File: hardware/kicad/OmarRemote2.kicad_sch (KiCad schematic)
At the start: 17 parts, among them J1 Conn_01x02_Pin, SW1 SW_Push, SW2 SW_Push, SW3 SW_Push, SW4 SW_Push, SW5 SW_Push, SW6 SW_Push, U1 XIAO-ESP32-S3-SMD

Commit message: further work on TP4056 footprint
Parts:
- removed BC2: Battery Charger, symbol TP4056_USB-C_Protect_Module:TP4056_USB-C_Protect_Module
- added BC1: Battery Charger, symbol TP4056_USB-C_Protect_Module:TP4056_USB-C_Protect_Module
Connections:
- net BAT+: now also BC1. (OUT-); no longer R4.2, U1.15 (BAT)
- net BAT-: now also BC1. (OUT-); no longer R3.1, U1.16 (GND)
- new net OUT+: BC1. (OUT-), R4.2, U1.15 (BAT)
- new net OUT-: BC1. (OUT-), R3.1, U1.16 (GND)
- no-connect marks 2 -> 0

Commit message: update libaries
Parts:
- removed IR1: KY-005, symbol KY-005_IR:KY-005_IR_Sender
- removed U1: XIAO-ESP32-S3-SMD, symbol Seeed_Studio_XIAO_Series:XIAO-ESP32-C6-SMD
- added IR?: KY-005, symbol CustomLibary:KY-005_IR_Sender
- added U?: XIAO-ESP32-S3-SMD, CustomLibrary:XIAO-ESP32C6-SMD, symbol CustomLibary:XIAO-ESP32-C6-SMD
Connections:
- net 5V: now also IR?.2 (Vcc), U?.14 (5V)
- net ButtonBACK: now also U?.2 (GPIO1_A1_D1)
- net ButtonDOWN: now also U?.4 (GPIO21_D3)
- net ButtonLEFT: now also U?.6 (GPIO23_D5_SCL)
- net ButtonOK: now also U?.1 (GPIO0_A0_D0)
- net ButtonRIGHT: now also U?.5 (GPIO22_D4_SDA)
- net ButtonUP: now also U?.3 (GPIO2_A2_D2)
- net GND: now also IR?.3 (GND), U?.13 (GND)
- net IR: now also IR?.1 (INPUT), U?.7 (GPIO16_D6_TX)
- net LEDCharge: now also U?.9 (GPIO19_D8_SCK)
- net LEDPower: now also U?.8 (GPIO17_D7_RX)
- net OUT+: now also U?.15 (BAT)
- net OUT-: now also U?.16 (GND)
- net VoltBattery: now also U?.10 (GPIO20_D9_MISO)
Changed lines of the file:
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@@
+	)
+	(symbol
+		(lib_id "CustomLibary:XIAO-ESP32-C6-SMD")
+		(at 143.51 52.07 0)
+		(unit 1)
+		(exclude_from_sim no)
+		(in_bom yes)
+		(on_board yes)
+		(dnp no)
+		(fields_autoplaced yes)
+		(property "Reference" "U?"
+			(at 148.1933 73.66 0)
+			(effects
+				(font
+					(size 1.27 1.27)
+				)
+				(justify left)
+			)
+		)
+		(property "Value" "XIAO-ESP32-S3-SMD"
+			(at 148.1933 76.2 0)
+			(effects
+				(font
+					(size 1.27 1.27)
+				)
+				(justify left)
+			)
+		)
+		(property "Footprint" "CustomLibrary:XIAO-ESP32C6-SMD"
+			(at 134.62 46.99 0)
+			(effects
+				(font
+					(size 1.27 1.27)
+				)
+				(hide yes)
+			)
+		)
+		(property "Datasheet" ""
+			(at 134.62 46.99 0)
+			(effects
+				(font
+					(size 1.27 1.27)
+				)
+				(hide yes)
+			)
+		)
+		(property "Description" ""
+			(at 143.51 52.07 0)
+			(effects
+				(font
+					(size 1.27 1.27)
+				)
+				(hide yes)
+			)
+		)
+		(pin "22"
+		)
+		(pin "16"
+		)
+		(pin "21"
+		)
+		(pin "20"
+		)
+		(pin "15"
+		)
+		(pin "19"
+		)
+		(pin "18"
+		)
+		(pin "17"
+		)
+		(pin "7"
+		)
+		(pin "6"
+		)
+		(pin "5"
+		)
+		(pin "4"
+		)
+		(pin "3"
+		)
+		(pin "2"
+		)
+		(pin "1"
+		)
+		(pin "24"
+		)
+		(pin "14"
+		)
+		(pin "13"
+		)
+		(pin "12"
+		)
+		(pin "23"
+		)
+		(pin "11"
+		)
+		(pin "10"
+		)
+		(pin "9"
+		)
+		(pin "8"
+		)
+		(instances
+			(project ""
+				(path "/1bf0dd3a-ef06-4d9e-bc1a-d833f6081a87"
+					(reference "U?")
+					(unit 1)
+				)
+			)
+		)
 	)
 	(symbol
@@
 	)
 	(symbol
-		(lib_id "Seeed_Studio_XIAO_Series:XIAO-ESP32-C6-SMD")
-		(at 143.51 52.07 0)
-		(unit 1)
-		(exclude_from_sim no)
-		(in_bom yes)
-		(on_board yes)
-		(dnp no)
-		(fields_autoplaced yes)
-		(property "Reference" "U1"
-			(at 148.1933 73.66 0)
-			(effects
-				(font
-					(size 1.27 1.27)
-				)
-				(justify left)
-			)
-		)
-		(property "Value" "XIAO-ESP32-S3-SMD"
-			(at 148.1933 76.2 0)
-			(effects
-				(font
-					(size 1.27 1.27)
-				)
-				(justify left)
-			)
-		)
-		(property "Footprint" ""
-			(at 134.62 46.99 0)
-			(effects
-				(font
-					(size 1.27 1.27)
-				)
-				(hide yes)
-			)
-		)
-		(property "Datasheet" ""
-			(at 134.62 46.99 0)
-			(effects
-				(font
-					(size 1.27 1.27)
-				)
-				(hide yes)
-			)
-		)
-		(property "Description" ""
-			(at 143.51 52.07 0)
-			(effects
-				(font
-					(size 1.27 1.27)
-				)
-				(hide yes)
-			)
-		)
-		(pin "23"
-		)
-		(pin "3"
-		)
-		(pin "10"
-		)
-		(pin "1"
-		)
-		(pin "17"
-		)
-		(pin "22"
-		)
-		(pin "2"
-		)
-		(pin "11"
-		)
-		(pin "13"
-		)
-		(pin "4"
-		)
-		(pin "16"
-		)
-		(pin "20"
-		)
-		(pin "7"
-		)
-		(pin "5"
-		)
-		(pin "6"
-		)
-		(pin "19"
-		)
-		(pin "8"
-		)
-		(pin "9"
-		)
-		(pin "15"
-		)
-		(pin "14"
-		)
-		(pin "18"
-		)
-		(pin "24"
-		)
-		(pin "12"
-		)
-		(pin "21"
-		)
-		(instances
-			(project ""
-				(path "/1bf0dd3a-ef06-4d9e-bc1a-d833f6081a87"
-					(reference "U1")
-					(unit 1)
-				)
-			)
-		)
-	)
-	(symbol
 		(lib_id "TP4056_USB-C_Protect_Module:TP4056_USB-C_Protect_Module")
 		(at 81.28 163.83 0)
@@
 	)
 	(symbol
-		(lib_id "KY-005_IR:KY-005_IR_Sender")
+		(lib_id "CustomLibary:KY-005_IR_Sender")
 		(at 129.54 105.41 0)
 		(unit 1)
@@
 		(dnp no)
 		(fields_autoplaced yes)
-		(property "Reference" "IR1"
+		(property "Reference" "IR?"
 			(at 135.89 100.33 0)
 			(effects
@@
 			)
 		)
-		(pin "1"
-		)
 		(pin "2"
 		)
 		(pin "3"
 		)
-		(instances
-			(project ""
-				(path "/1bf0dd3a-ef06-4d9e-bc1a-d833f6081a87"
-					(reference "IR1")
-					(unit 1)
-				)
+		(pin "1"
+		)
+		(instances
+			(project ""
+				(path "/1bf0dd3a-ef06-4d9e-bc1a-d833f6081a87"
+					(reference "IR?")
+					(unit 1)
+				)

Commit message: steal subsheets from @MayNiklas
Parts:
- removed J1: Conn_01x02_Pin, symbol Connector:Conn_01x02_Pin
- gave numbers to parts that had none: 2
- renumbered R3 to R1, R4 to R2, R1 to R3, R2 to R4
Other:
- added sheet USB-C charging (USB.kicad_sch)
- added sheet battery protection (battery_protection.kicad_sch)
- added sheet charging (charging.kicad_sch)

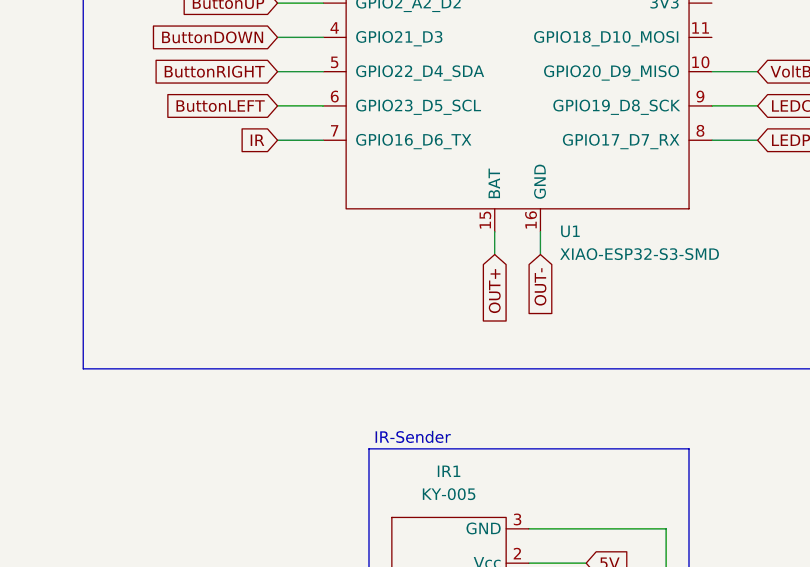
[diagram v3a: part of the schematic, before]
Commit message: add switch
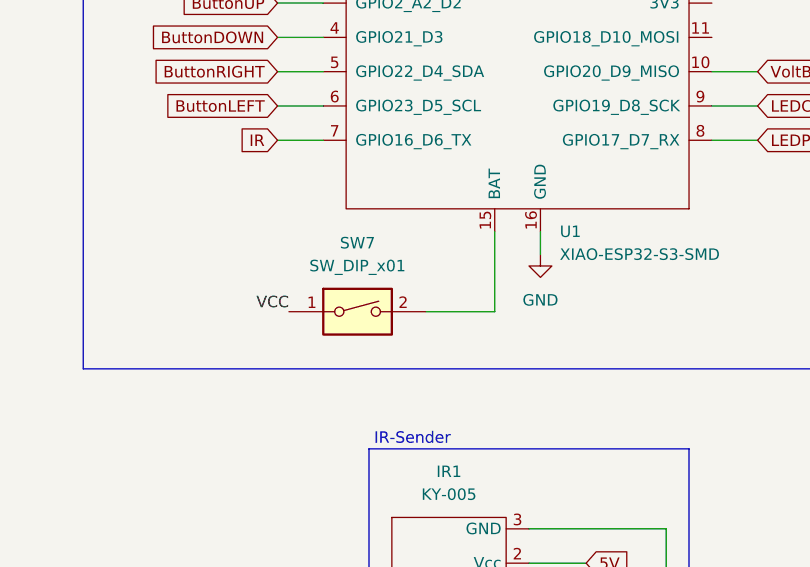
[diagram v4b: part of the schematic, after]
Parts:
- added SW7: SW_DIP_x01, symbol Switch:SW_DIP_x01
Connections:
- net GND: now also U1.16 (GND)
- net OUT+: no longer U1.15 (BAT)
- net OUT-: no longer U1.16 (GND)
- net VCC: now also SW7.1
- new net: SW7.2, U1.15 (BAT)

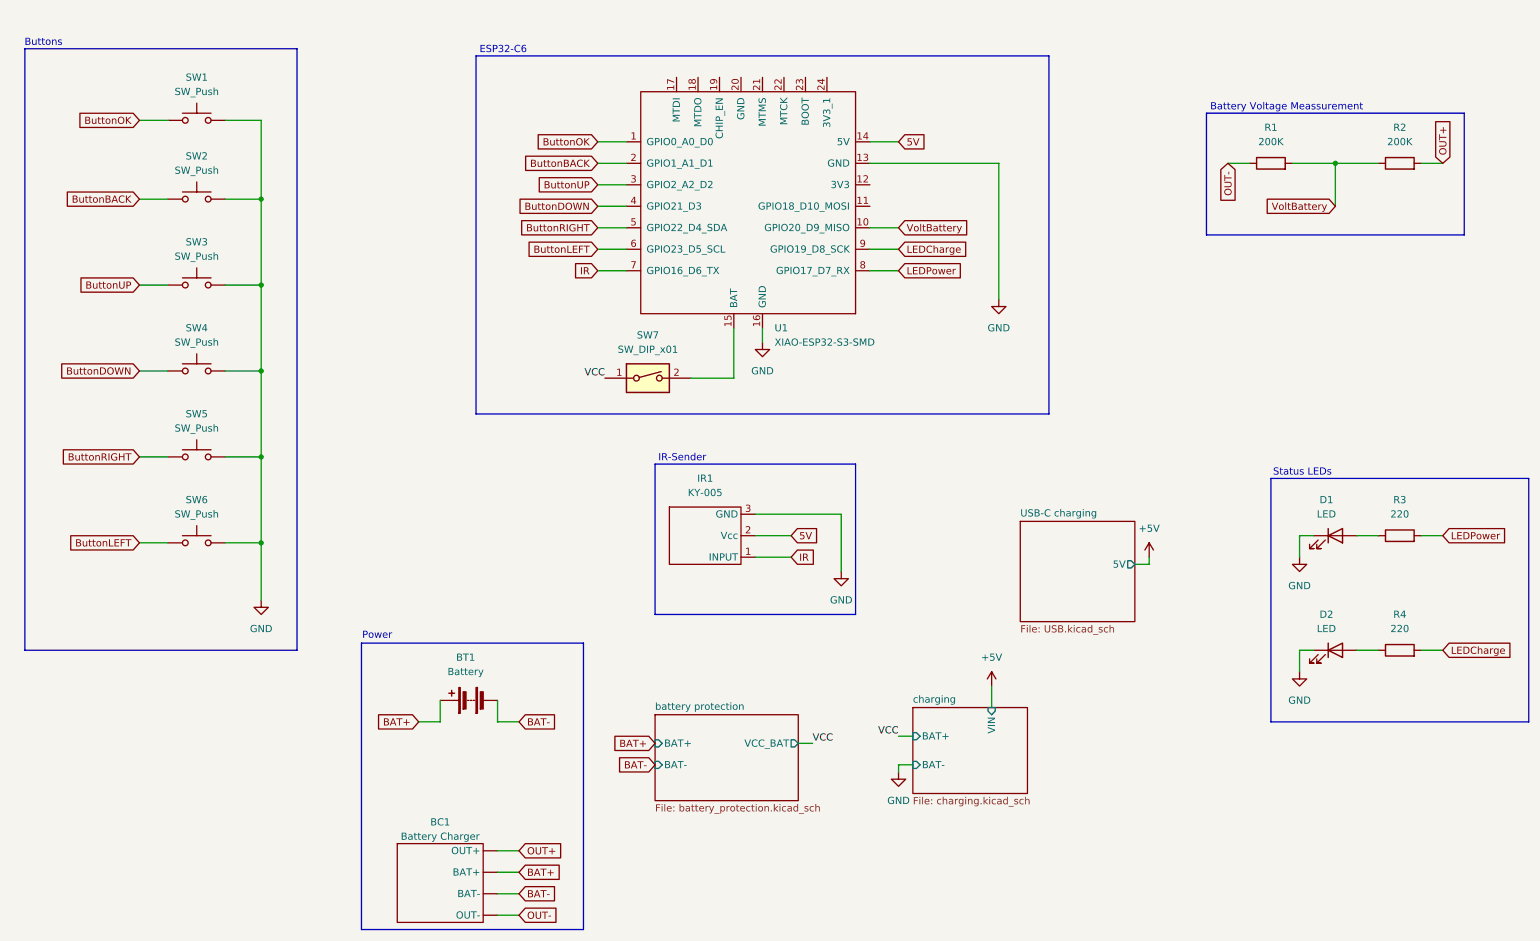
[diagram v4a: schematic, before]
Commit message: fix voltage measurement
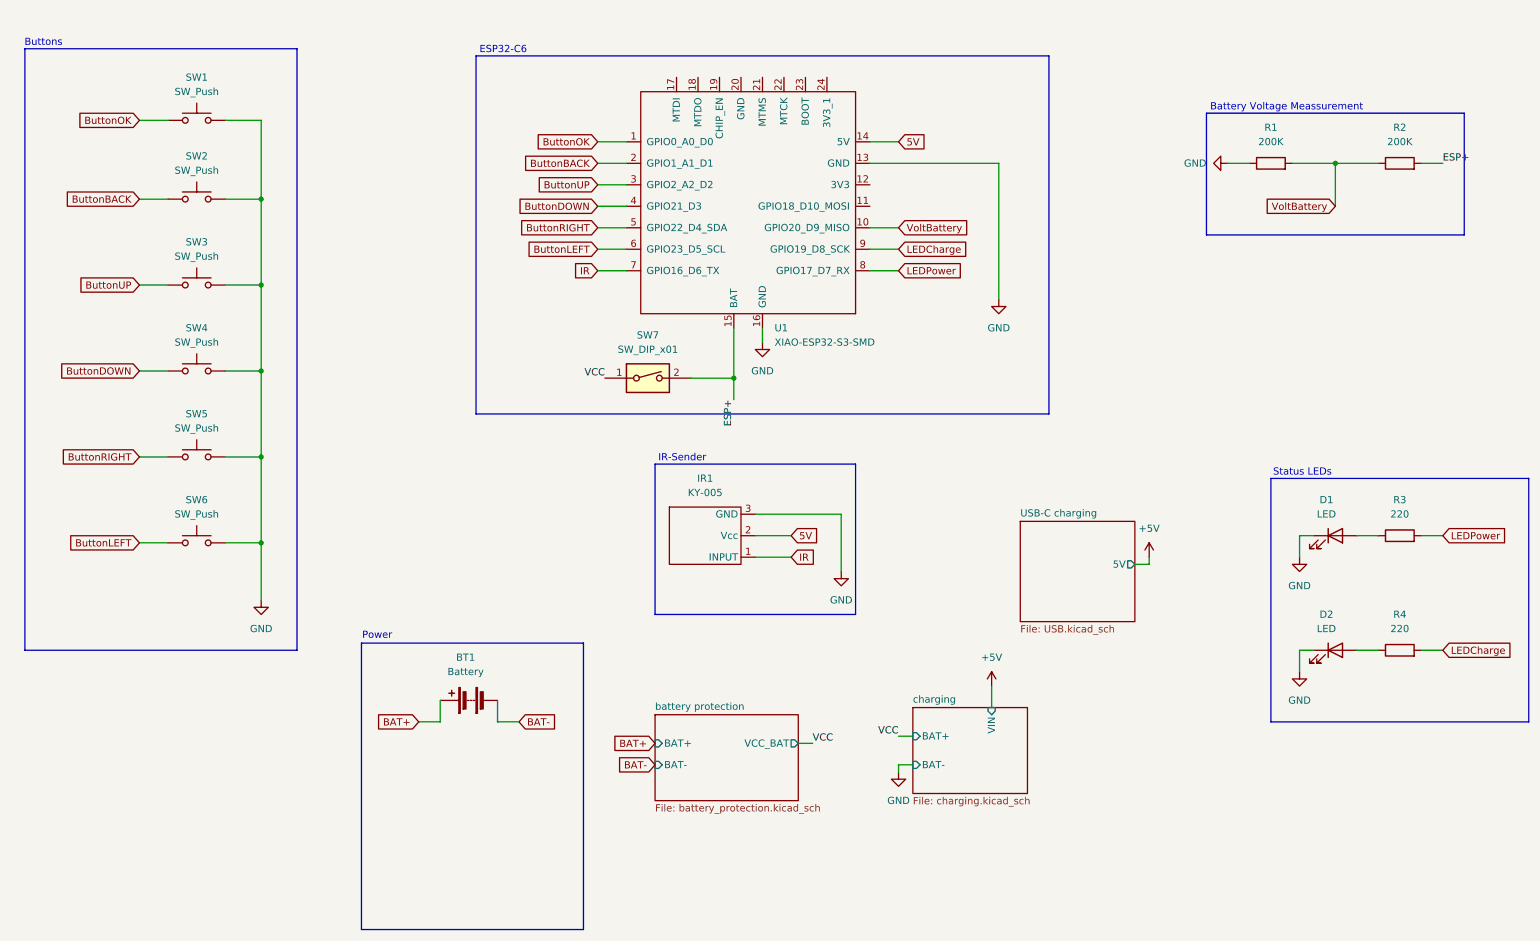
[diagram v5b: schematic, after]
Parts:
- removed BC1: Battery Charger, symbol TP4056_USB-C_Protect_Module:TP4056_USB-C_Protect_Module
- SW1, SW2, SW3, SW4, SW5, SW6: footprint (none) -> CustomLibrary:SW-TH_4P-L6.0-W6.0-P4.50-LS6.5
- SW7: footprint (none) -> Connector_JST:JST_XH_B2B-XH-AM_1x02_P2.50mm_Vertical
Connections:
- net OUT+ is gone; now on net ESP+: R2.2
- net OUT- is gone; now on net GND: R1.1
- net ESP+: now reaches SW7.2, U1.15 (BAT)
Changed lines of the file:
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@@
+	)
+	(junction
+		(at 140.97 82.55)
+		(diameter 0)
+		(color 0 0 0 0)
 	)
 	(junction
@@
 	(wire
 		(pts
+			(xy 140.97 86.36) (xy 140.97 82.55)
+		)
+		(stroke
+			(width 0)
+			(type default)
+		)
+	)
+	(wire
+		(pts
 			(xy 57.15 81.28) (xy 57.15 96.52)
 		)
@@
 	(wire
 		(pts
-			(xy 99.06 170.18) (xy 102.87 170.18)
-		)
-		(stroke
-			(width 0)
-			(type default)
-		)
-	)
-	(wire
-		(pts
-			(xy 140.97 82.55) (xy 133.35 82.55)
+			(xy 133.35 82.55) (xy 140.97 82.55)
 		)
 		(stroke
@@
 	(wire
 		(pts
-			(xy 99.06 173.99) (xy 102.87 173.99)
-		)
-		(stroke
-			(width 0)
-			(type default)
-		)
-	)
-	(wire
-		(pts
 			(xy 170.18 151.13) (xy 172.72 151.13)
 		)
@@
 	(wire
 		(pts
-			(xy 99.06 177.8) (xy 102.87 177.8)
-		)
-		(stroke
-			(width 0)
-			(type default)
-		)
-	)
-	(wire
-		(pts
 			(xy 57.15 96.52) (xy 57.15 111.76)
 		)
@@
 	(wire
 		(pts
-			(xy 99.06 166.37) (xy 102.87 166.37)
-		)
-		(stroke
-			(width 0)
-			(type default)
-		)
-	)
-	(wire
-		(pts
 			(xy 99.06 143.51) (xy 102.87 143.51)
 		)
@@
 			(width 0)
 			(type default)
+		)
+	)
+	(label "ESP+"
+		(at 266.7 44.45 0)
+		(effects
+			(font
+				(size 1.27 1.27)
+			)
+			(justify left bottom)
+		)
+	)
+	(label "ESP+"
+		(at 140.97 86.36 270)
+		(effects
+			(font
+				(size 1.27 1.27)
+			)
+			(justify right bottom)
 		)
 	)
@@
 		)
 	)
-	(global_label "OUT-"
-		(shape input)
-		(at 102.87 177.8 0)
-		(fields_autoplaced yes)
-		(effects
-			(font
-				(size 1.27 1.27)
-			)
-			(justify left)
-		)
-		(property "Intersheetrefs" "${INTERSHEET_REFS}"
-			(at 111.0562 177.8 0)
-			(effects
-				(font
-					(size 1.27 1.27)
-				)
-				(justify left)
-				(hide yes)
-			)
-		)
-	)
 	(global_label "ButtonUP"
 		(shape input)
@@
 		)
 	)
-	(global_label "OUT-"
-		(shape input)
-		(at 228.6 44.45 270)
-		(fields_autoplaced yes)
-		(effects
-			(font
-				(size 1.27 1.27)
-			)
-			(justify right)
-		)
-		(property "Intersheetrefs" "${INTERSHEET_REFS}"
-			(at 228.6 52.6362 90)
-			(effects
-				(font
-					(size 1.27 1.27)
-				)
-				(justify right)
-				(hide yes)
-			)
-		)
-	)
 	(global_label "5V"
 		(shape input)
@@
 		)
 	)
-	(global_label "BAT-"
-		(shape input)
-		(at 102.87 173.99 0)
-		(fields_autoplaced yes)
-		(effects
-			(font
-				(size 1.27 1.27)
-			)
-			(justify left)
-		)
-		(property "Intersheetrefs" "${INTERSHEET_REFS}"
-			(at 110.7538 173.99 0)
-			(effects
-				(font
-					(size 1.27 1.27)
-				)
-				(justify left)
-				(hide yes)
-			)
-		)
-	)
-	(global_label "BAT+"
-		(shape input)
-		(at 102.87 170.18 0)
-		(fields_autoplaced yes)
-		(effects
-			(font
-				(size 1.27 1.27)
-			)
-			(justify left)
-		)
-		(property "Intersheetrefs" "${INTERSHEET_REFS}"
-			(at 110.7538 170.18 0)
-			(effects
-				(font
-					(size 1.27 1.27)
-				)
-				(justify left)
-				(hide yes)
-			)
-		)
-	)
 	(global_label "BAT+"
 		(shape input)
@@
 		)
 	)
-	(global_label "OUT+"
-		(shape input)
-		(at 102.87 166.37 0)
-		(fields_autoplaced yes)
-		(effects
-			(font
-				(size 1.27 1.27)
-			)
-			(justify left)
-		)
-		(property "Intersheetrefs" "${INTERSHEET_REFS}"
-			(at 111.0562 166.37 0)
-			(effects
-				(font
-					(size 1.27 1.27)
-				)
-				(justify left)
-				(hide yes)
-			)
-		)
-	)
 	(global_label "LEDPower"
 		(shape input)
@@
 				)
 				(justify right)
-				(hide yes)
-			)
-		)
-	)
-	(global_label "OUT+"
-		(shape input)
-		(at 266.7 44.45 90)
-		(fields_autoplaced yes)
-		(effects
-			(font
-				(size 1.27 1.27)
-			)
-			(justify left)
-		)
-		(property "Intersheetrefs" "${INTERSHEET_REFS}"
-			(at 266.7 36.2638 90)
-			(effects
-				(font
-					(size 1.27 1.27)
-				)
-				(justify left)
 				(hide yes)
 			)
@@
 			)
 		)
-		(property "Footprint" ""
+		(property "Footprint" "CustomLibrary:SW-TH_4P-L6.0-W6.0-P4.50-LS6.5"
 			(at 45.72 76.2 0)
 			(effects
@@
 			)
 		)
-		(property "Footprint" ""
+		(property "Footprint" "CustomLibrary:SW-TH_4P-L6.0-W6.0-P4.50-LS6.5"
 			(at 45.72 106.68 0)
 			(effects
@@
 			)
 		)
-		(property "Footprint" ""
+		(property "Footprint" "CustomLibrary:SW-TH_4P-L6.0-W6.0-P4.50-LS6.5"
 			(at 45.72 60.96 0)
 			(effects
@@
 				(path "/1bf0dd3a-ef06-4d9e-bc1a-d833f6081a87"
 					(reference "SW3")
-					(unit 1)
-				)
-			)
-		)
-	)
-	(symbol
-		(lib_id "TP4056_USB-C_Protect_Module:TP4056_USB-C_Protect_Module")
-		(at 81.28 163.83 0)
-		(unit 1)
-		(exclude_from_sim no)
-		(in_bom yes)
-		(on_board yes)
-		(dnp no)
-		(fields_autoplaced yes)
-		(property "Reference" "BC1"
-			(at 88.9 161.29 0)
-			(effects
-				(font
-					(size 1.27 1.27)
-				)
-			)
-		)
-		(property "Value" "Battery Charger"
-			(at 88.9 163.83 0)
-			(effects
-				(font
-					(size 1.27 1.27)
-				)
-			)
-		)
-		(property "Footprint" ""
-			(at 81.28 163.83 0)
-			(effects
-				(font
-					(size 1.27 1.27)
-				)
-				(hide yes)
-			)
-		)
-		(property "Datasheet" ""
-			(at 81.28 163.83 0)
-			(effects
-				(font
-					(size 1.27 1.27)
-				)
-				(hide yes)
-			)
-		)
-		(property "Description" ""
-			(at 81.28 163.83 0)
-			(effects
-				(font
-					(size 1.27 1.27)
-				)
-				(hide yes)
-			)
-		)
-		(pin ""
-		)
-		(pin ""
-		)
-		(pin ""
-		)
-		(pin ""
-		)
-		(instances
-			(project ""
-				(path "/1bf0dd3a-ef06-4d9e-bc1a-d833f6081a87"
-					(reference "BC1")
 					(unit 1)
 				)
@@
 			)
 		)
-		(property "Footprint" ""
+		(property "Footprint" "Connector_JST:JST_XH_B2B-XH-AM_1x02_P2.50mm_Vertical"
 			(at 125.73 82.55 0)
 			(effects
@@
 			)
 		)
-		(property "Footprint" ""
+		(property "Footprint" "CustomLibrary:SW-TH_4P-L6.0-W6.0-P4.50-LS6.5"
 			(at 45.72 45.72 0)
 			(effects
@@
 				(path "/1bf0dd3a-ef06-4d9e-bc1a-d833f6081a87"
 					(reference "SW2")
+					(unit 1)
+				)
+			)
+		)
+	)
+	(symbol
+		(lib_id "power:GND")
+		(at 228.6 44.45 270)
+		(unit 1)
+		(exclude_from_sim no)
+		(in_bom yes)
+		(on_board yes)
+		(dnp no)
+		(fields_autoplaced yes)
+		(property "Reference" "#PWR012"
+			(at 222.25 44.45 0)
+			(effects
+				(font
+					(size 1.27 1.27)
+				)
+				(hide yes)
+			)
+		)
+		(property "Value" "GND"
+			(at 224.79 44.4499 90)
+			(effects
+				(font
+					(size 1.27 1.27)
+				)
+				(justify right)
+			)
+		)
+		(property "Footprint" ""
+			(at 228.6 44.45 0)
+			(effects
+				(font
+					(size 1.27 1.27)
+				)
+				(hide yes)
+			)
+		)
+		(property "Datasheet" ""
+			(at 228.6 44.45 0)
+			(effects
+				(font
+					(size 1.27 1.27)
+				)
+				(hide yes)
+			)
+		)
+		(property "Description" "Power symbol creates a global label with name \"GND\" , ground"
+			(at 228.6 44.45 0)
+			(effects
+				(font
+					(size 1.27 1.27)
+				)
+				(hide yes)
+			)
+		)
+		(pin "1"
+		)
+		(instances
+			(project "OmarRemote2"
+				(path "/1bf0dd3a-ef06-4d9e-bc1a-d833f6081a87"
+					(reference "#PWR012")
 					(unit 1)
 				)
@@
 			)
 		)
-		(property "Footprint" ""
+		(property "Footprint" "CustomLibrary:SW-TH_4P-L6.0-W6.0-P4.50-LS6.5"
 			(at 45.72 91.44 0)
 			(effects
@@
 			)
 		)
-		(property "Footprint" ""
+		(property "Footprint" "CustomLibrary:SW-TH_4P-L6.0-W6.0-P4.50-LS6.5"
 			(at 45.72 31.75 0)
 			(effects

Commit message: start work on pcb layout
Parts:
- removed D1, D2: LED, symbol Device:LED
- removed IR1: KY-005, symbol CustomLibary:KY-005_IR_Sender
- removed R3, R4: 220, symbol Device:R
- added J2: Conn_01x03, Connector_JST:JST_XH_B3B-XH-A_1x03_P2.50mm_Vertical, symbol Connector_Generic:Conn_01x03
- R1, R2: footprint (none) -> Resistor_SMD:R_0805_2012Metric
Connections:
- net 5V: now also J2.2 (Pin_2)
- net GND: now also J2.3 (Pin_3)
- net IR: now also J2.1 (Pin_1)
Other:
- note removed: "Status LEDs"
- company: Afeef -> Niklas Steffen, Afeef Neiroukh
- moved on the sheet: BT1, R1, R2
